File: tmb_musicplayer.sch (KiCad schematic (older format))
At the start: 0 parts

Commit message: new layout
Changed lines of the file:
@@
 F9 "VS_UART_RX" I R 3250 1150 60
 F10 "VS_UART_TX" O R 3250 1250 60
-F11 "VS_SDA" I R 3250 1350 60
-F12 "VS_SCL" I R 3250 1450 60
-F13 "VS_I2S_LROUT" I R 3250 1800 60
-F14 "VS_I2S_MCLK" I R 3250 1900 60
-F15 "VS_I2S_SCLK" I R 3250 2000 60
-F16 "VS_I2S_SDATA" I R 3250 2100 60
+F11 "VS_I2S_LROUT" I R 3250 1800 60
+F12 "VS_I2S_MCLK" I R 3250 1900 60
+F13 "VS_I2S_SCLK" I R 3250 2000 60
+F14 "VS_I2S_SDATA" I R 3250 2100 60
 $EndSheet
 $Sheet
@@
 Text Label 3650 4050 0    60   ~ 0
 PD7
-Text Label 3600 1350 0    60   ~ 0
-PB7
-Text Label 3600 1450 0    60   ~ 0
-PB6
 Text Label 8450 4050 0    60   ~ 0
 PB6
@@
 	3650 4050 3250 4050
 Wire Wire Line
-	3600 1450 3250 1450
-Wire Wire Line
-	3250 1350 3600 1350
-Wire Wire Line
 	8450 4150 8000 4150

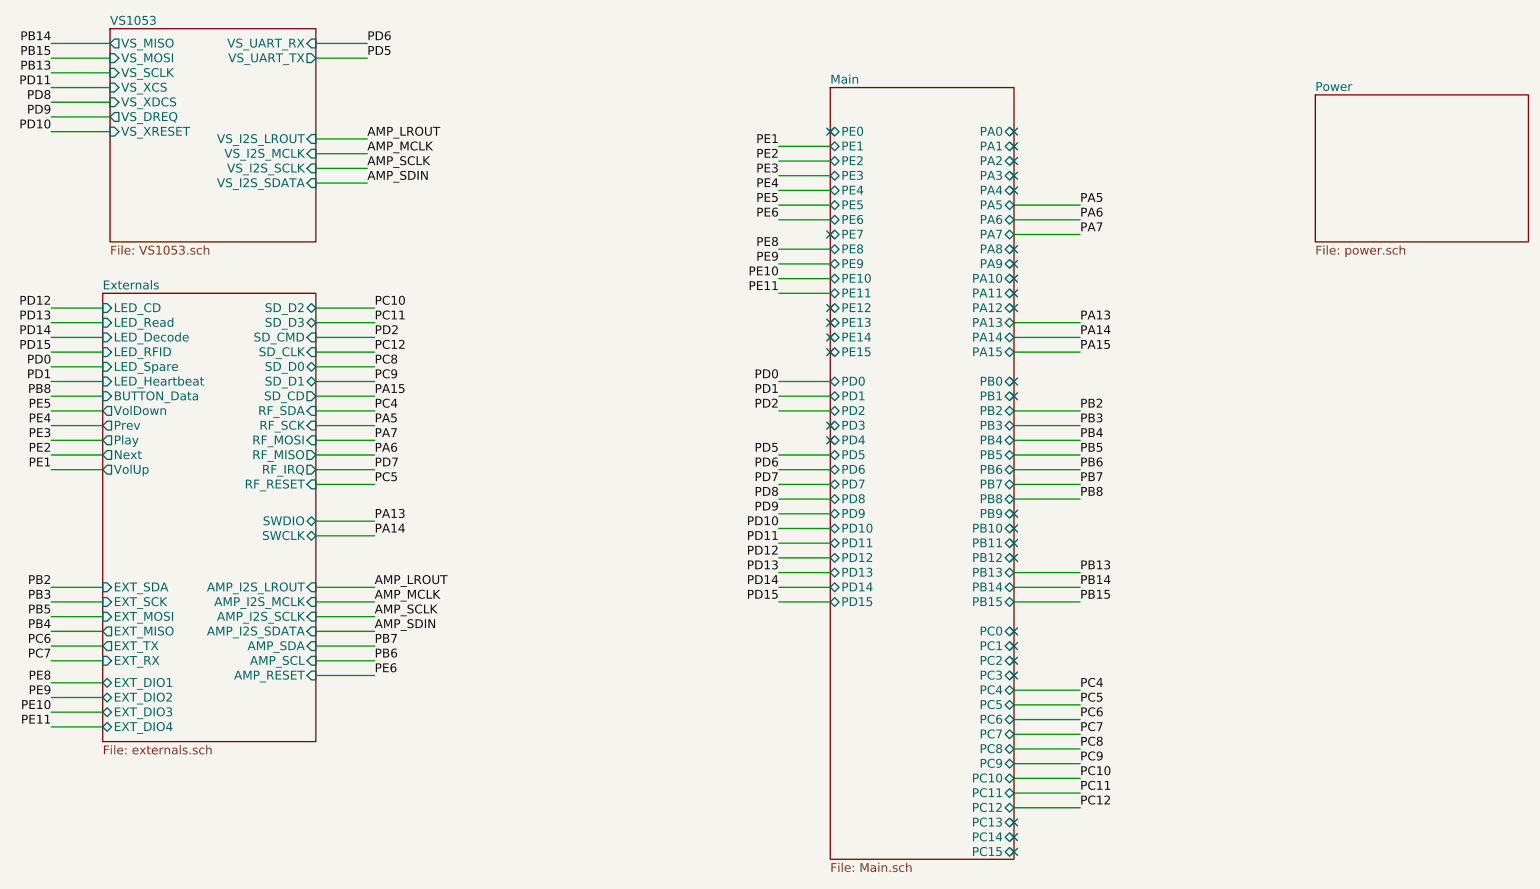
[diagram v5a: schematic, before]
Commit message: Remove 3. LDO some improvements
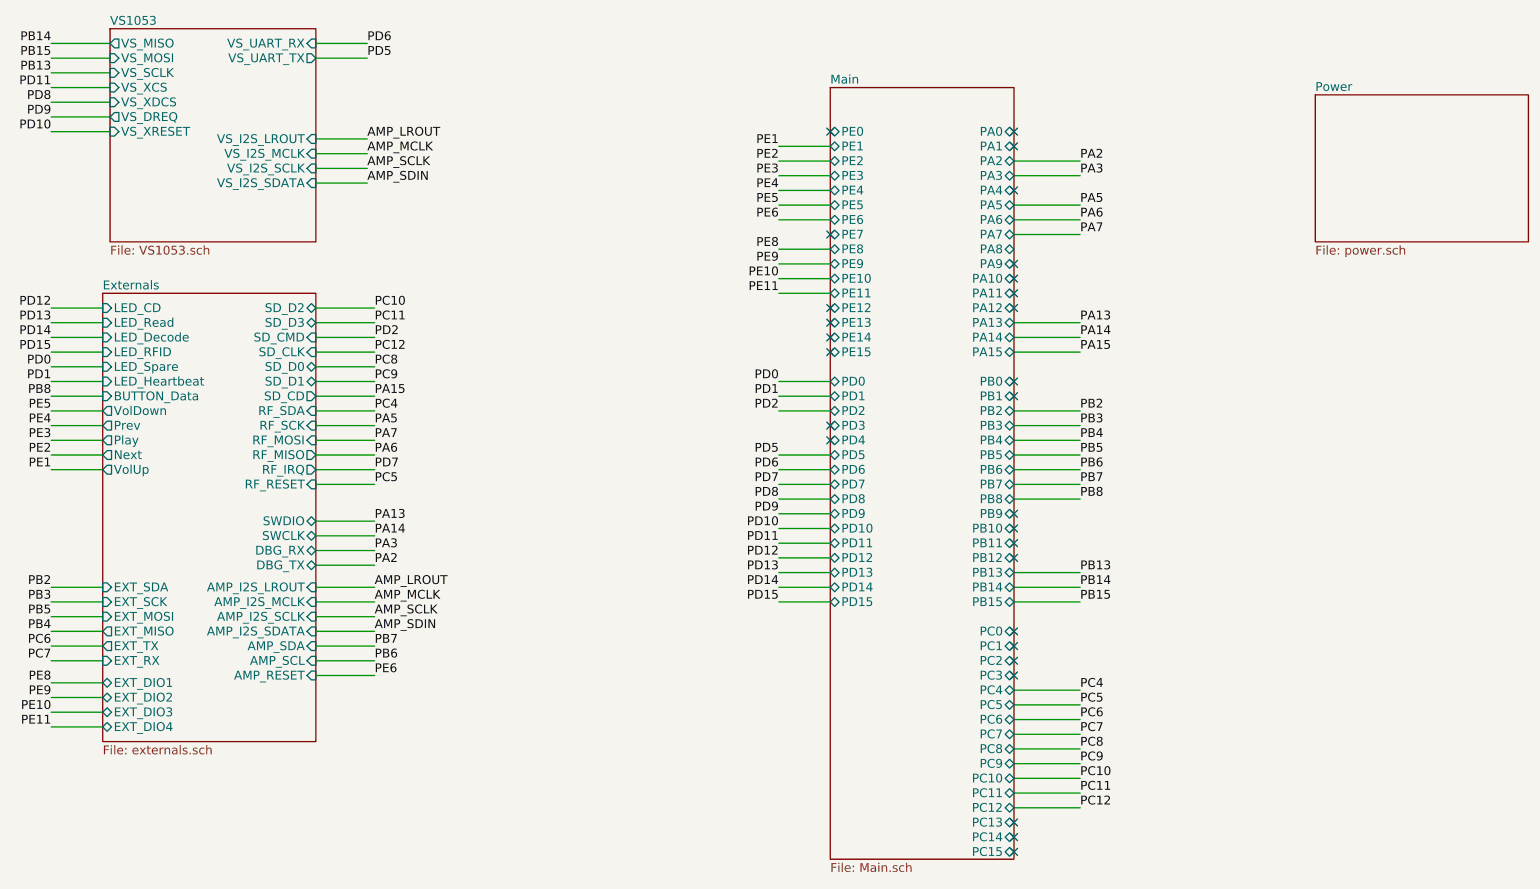
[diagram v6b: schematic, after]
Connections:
- no-connect marks 31 -> 28
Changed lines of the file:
@@
 LIBS:MF_Connectors
 LIBS:misc
+LIBS:switches
 LIBS:tmb_musicplayer-cache
 EELAYER 25 0
@@
 F44 "EXT_DIO3" B L 1800 5700 60
 F45 "EXT_DIO4" B L 1800 5800 60
+F46 "DBG_RX" B R 3250 4600 60
+F47 "DBG_TX" B R 3250 4700 60
 $EndSheet
 $Sheet
@@
 NoConn ~ 8000 1750
 NoConn ~ 8000 1850
-NoConn ~ 8000 1950
-NoConn ~ 8000 2050
 NoConn ~ 8000 2150
 NoConn ~ 8000 2750
 NoConn ~ 8000 2650
-NoConn ~ 8000 2550
 NoConn ~ 8000 2850
 NoConn ~ 8000 2950
@@
 NoConn ~ 8000 6550
 NoConn ~ 8000 6650
+Text Label 8450 1950 0    60   ~ 0
+PA2
+Text Label 8450 2050 0    60   ~ 0
+PA3
+Wire Wire Line
+	8000 1950 8450 1950
+Wire Wire Line
+	8000 2050 8450 2050
+Text Label 3650 4700 0    60   ~ 0
+PA2
+Wire Wire Line
+	3650 4700 3250 4700
+Text Label 3650 4600 0    60   ~ 0
+PA3
+Wire Wire Line
+	3650 4600 3250 4600
 $EndSCHEMATC
